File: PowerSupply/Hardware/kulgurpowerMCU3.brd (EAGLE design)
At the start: 102 x 57 mm, 135 parts, among them IC2 TPS77333DGK, IC3 REG1117-5, U1 MPU-6000QFN-24, U2 MPU-6000QFN-24, X1 12Mhz, X2 2534-, X3 22-23-2021

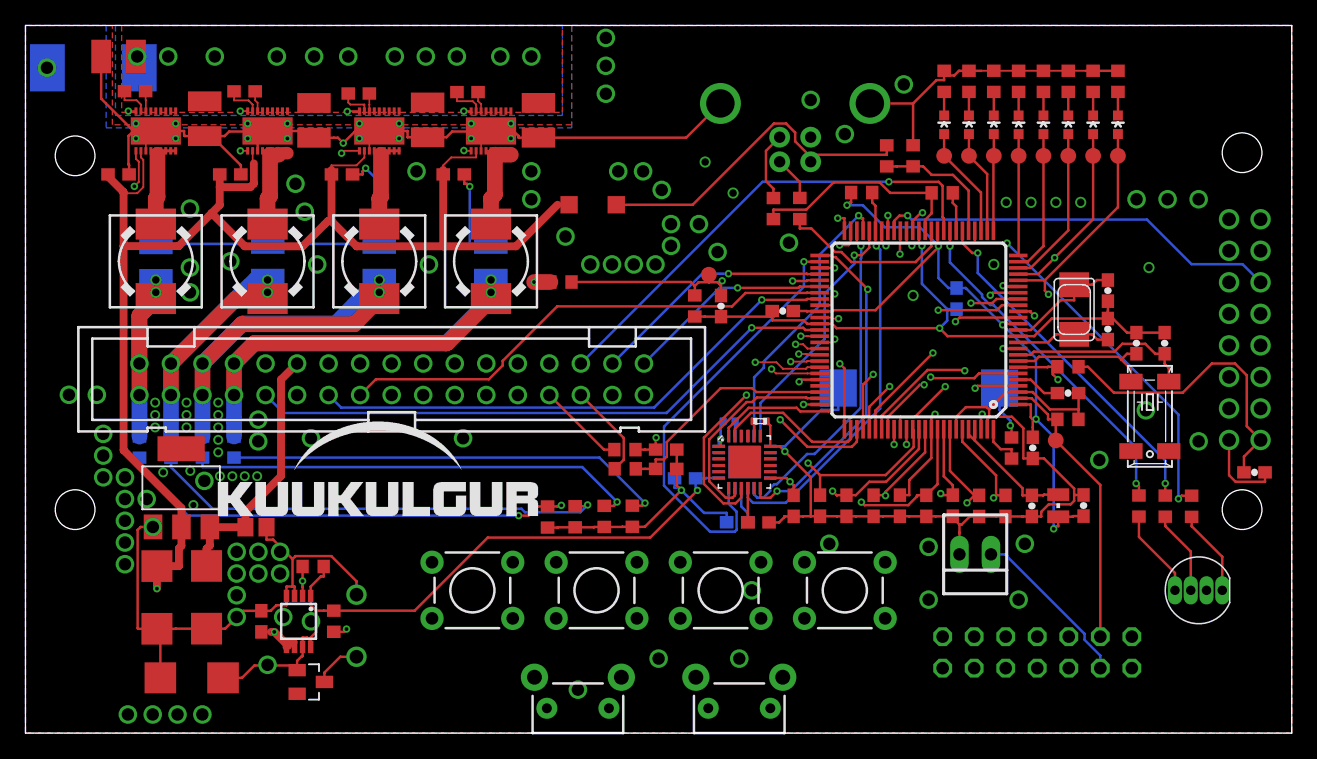
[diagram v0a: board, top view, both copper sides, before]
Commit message: Never MCU board of power supply in. 19.2Mhz oscillator added
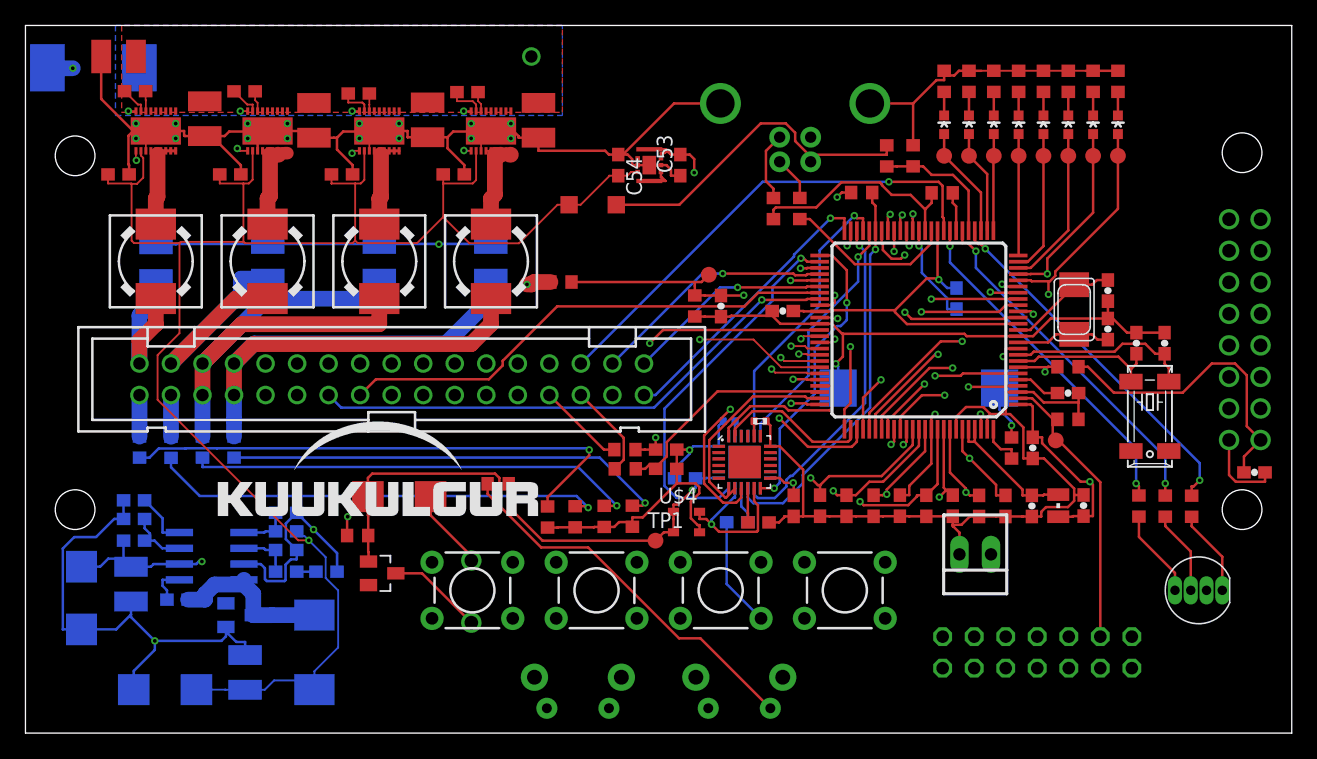
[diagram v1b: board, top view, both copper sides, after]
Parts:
- removed C16, C41: (no value), rcl:C/6032-28R
- removed C23: 1uF/ 26V, resistor:C0805
- removed IC2: TPS77333DGK, samuel:MSOP8
- removed IC3: REG1117-5, burr-brown:SOT223
- added C100: 100uF/10V, rcl:C/6032-28R
- added C51: 12pF, SparkFun:0603-CAP
- added C52: 180pF, SparkFun:0603-CAP
- added C53: 10uF / 6.3V, rcl:C0603
- added C54: 4.7uF / 10V, rcl:C0603
- added C55: 15nF, SparkFun:0603-CAP
- added C56, C57: GRM32ER71E226KE15L, rcl:C1210
- added C58: 100uF/16V, rcl:C/6032-28R
- added D100: BAT54, diode:SOT23
- added L7: 4,7uH, inductors:DR73
- added R20: 100k, SparkFun:0603-RES
- added R21: 63k4, SparkFun:0603-RES
- added R37: 1k87, SparkFun:0603-RES
- added R38: 10k, SparkFun:0603-RES
- added R45: 21k5, SparkFun:0603-RES
- added TP1: TPB1,27, testpad:B1,27
- added U$4: ASE, crystal:ASE
- added U$5: TPS54332, tonu:SO8
- added U$6: XCL202B331BR-G, XCL202:CL2025
- C28: value 1uF/6V -> 0.1; device resistor:C0603 -> SparkFun:0603-CAP
- moved C18 22.2 mm to (30.1, 19.0), turned to 180 degrees
- moved R22 16.3 mm to (38.1, 20.1)
- moved D7 10.5 mm to (28.7, 12.9)
- moved U$1 9.65 mm to (35.9, 11.4)
- moved R6 7.17 mm to (26.8, 15.9), turned to 0 degrees
- moved C28 6.97 mm to (12.2, 10.8), flipped to the bottom, turned to 0 degrees
- flipped S1 to the bottom
- flipped S9 to the bottom
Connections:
- new net ENABLE_PANDA: R20.1, R45.2, U$5.3
- new net LX: U$6.P$1, U$6.P$7
- new net N$109: C51.1, C52.1, U$5.6
- new net N$120: C52.2, R21.2
- new net N$121: C28.2, U$5.1
- new net N$125: R37.1, R38.2, U$5.5
- new net N$138: C28.1, D100.3, L7.1, U$5.8
- new net N$26: U$4.3, U1.11, U2.11
- new net N$5: U1.1
- new net N$7: U2.1
- new net N$96: C55.2, U$5.4
- net !RESET: no longer IC2.2
- net +3V3: now also C53.2, TP1.TP, U$4.1, U$4.4, U$6.P$3, U$6.P$8; no longer IC2.1, IC2.7, IC2.8
- net 5V: now also C100.+, C54.2, C57.1, L7.2, R38.1, U$6.P$6; no longer C16.+, C28.1, IC2.5, IC2.6, IC3.2
- net GND: now also C100.-, C51.2, C53.1, C54.1, C55.1, C56.2, C57.2, C58.-, D100.1, R21.1, R37.2, R45.1, U$4.2, U$5.7, U$6.P$2, U$6.P$5, U$6.PAD; no longer C16.-, C23.2, C28.2, C41.-, IC2.3, IC2.4, IC3.1, U1.1, U2.1
- net V+: now also C56.1, C58.+, R20.2, U$5.2; no longer C23.1, C41.+, IC3.3
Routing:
- net GND: track 540.7 -> 366.3 mm, vias 110 -> 6
- net +3V3: track 208.0 -> 123.3 mm, vias 9 -> 6
- net +19V: track 56.7 -> 20.1 mm
- net 5V: track 125.1 -> 140.7 mm, vias 2 -> 1
- net !RESET: track 88.6 -> 74.8 mm, vias 2 -> 1
- net N$138: track 0.00 -> 13.3 mm
- net N$26: track 0.00 -> 13.0 mm, vias 0 -> 1
- net V+: track 21.1 -> 31.2 mm, vias 0 -> 1
- net SUPERCAP: track 66.7 -> 60.1 mm
- net OUT4_EN: track 46.3 -> 39.8 mm
- net MD: track 70.3 -> 64.8 mm
- net ENABLE_PANDA: track 0.00 -> 4.98 mm
- net PGOOD2: track 28.1 -> 23.1 mm
- net INT_GYRO2: track 35.0 -> 30.4 mm
- net N$96: track 0.00 -> 4.55 mm
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- removed copper zone on layer 1, net GND
- removed copper zone on layer 16, net GND
